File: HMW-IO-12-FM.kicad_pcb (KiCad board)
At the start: 2 copper layers, 47 x 47 mm, 64 parts, among them IC1 ATmega32A-A, IC2 ATmega32A-M, IC3 MAX487E, IC4 MC34063AD, J1 Conn_01x04_Male, J2 Conn_01x04_Male, J3 Screw_Terminal_01x06, J4 BUS_Terminal, Q1 16Mhz

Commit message: Add files via upload
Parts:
- D3: footprint Diode_SMD:D_SMA_Handsoldering -> Diode_SMD:D_MELF
- L1: footprint Inductor_SMD:L_Bourns_SRN6045TA -> Inductor_SMD:L_Taiyo-Yuden_MD-4040
- moved L1 0.65 mm to (145.5, 75.1)
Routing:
- net Net-(D3-Pad1): track 10.6 -> 11.7 mm

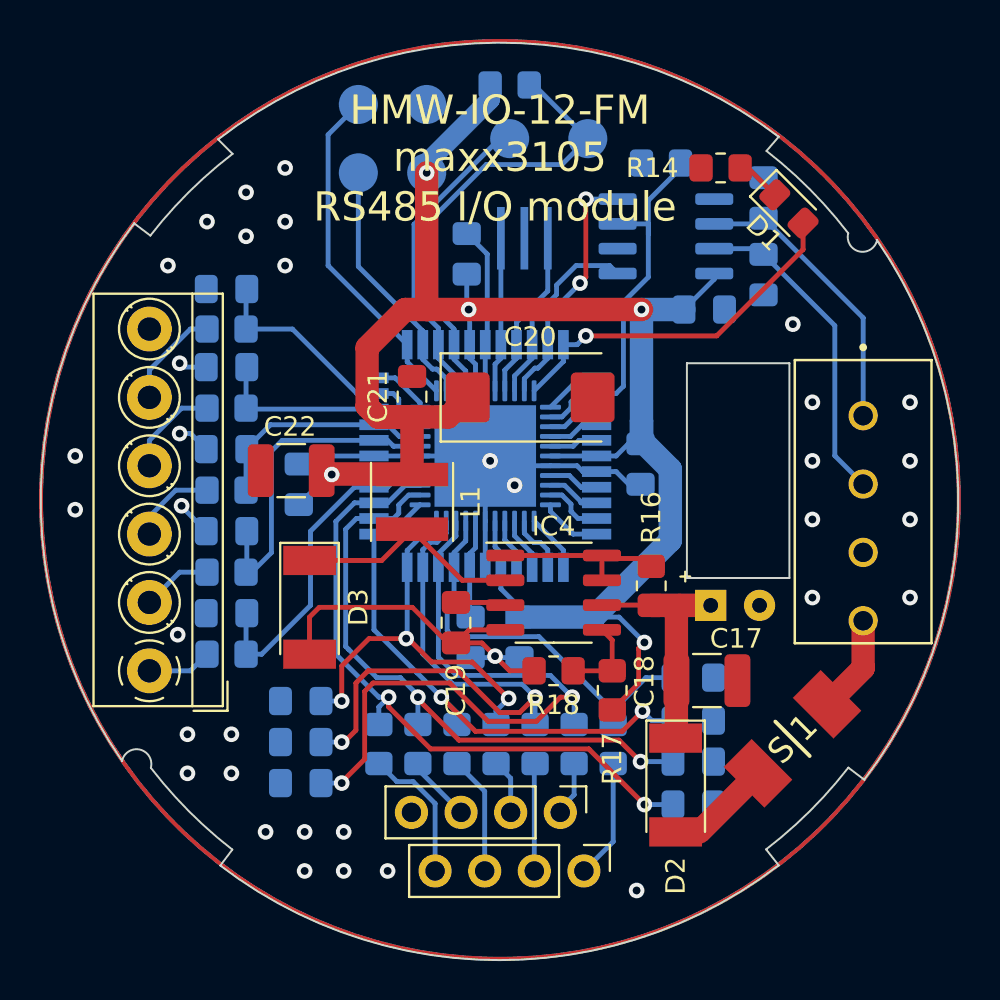
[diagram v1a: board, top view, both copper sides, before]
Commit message: Add files via upload
Bigger hole for tht capacitor.
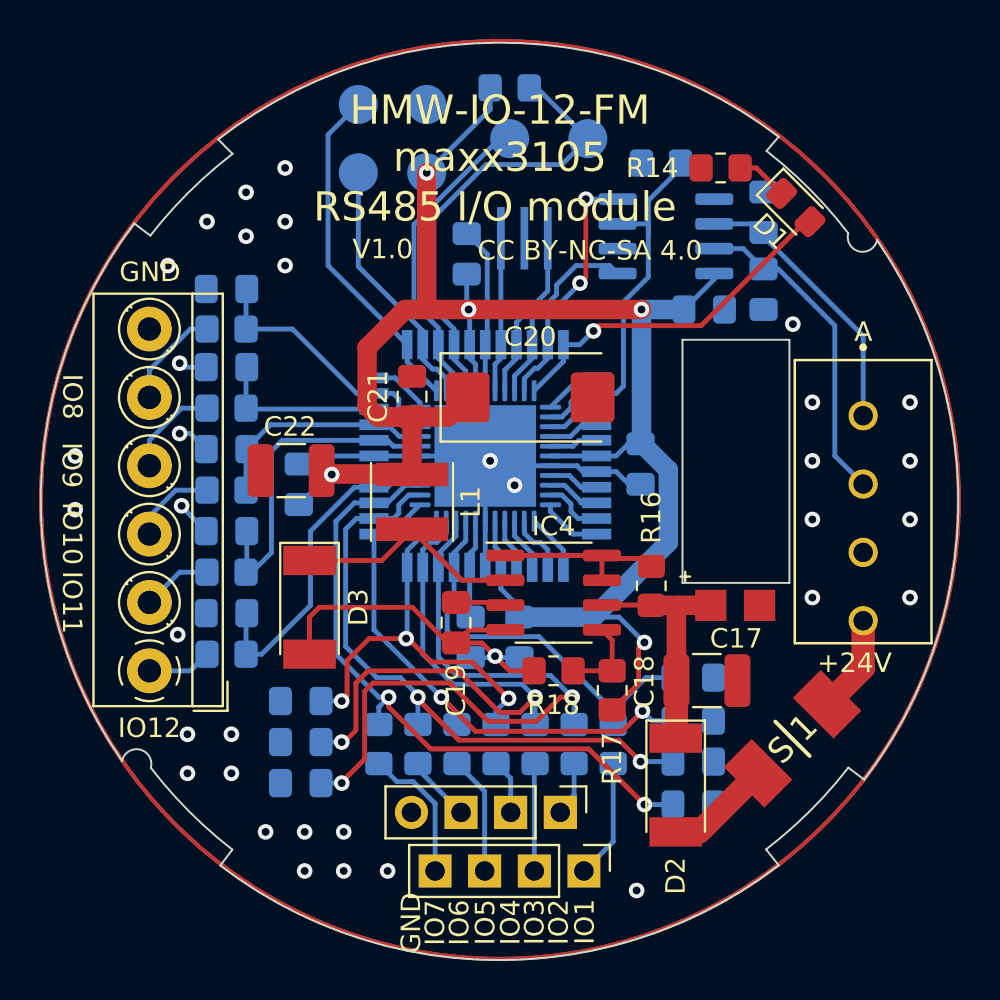
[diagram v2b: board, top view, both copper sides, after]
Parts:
- moved C14 0.75 mm to (163.5, 64.2)
- moved C15 0.73 mm to (163.5, 60.3)
- moved D1 0.36 mm to (165.2, 60.0)
- moved R13 0.15 mm to (150.5, 53.9)
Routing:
- net /GND: track 61.1 -> 58.6 mm
- net /VCC: track 104.0 -> 102.6 mm
- net Net-(D2-Pad2): track 5.46 -> 4.24 mm
- net Net-(J3-Pad3): track 4.31 -> 3.41 mm
- net Net-(C15-Pad1): track 14.9 -> 14.1 mm
- net /SO7: track 34.9 -> 34.2 mm
- net /SCK: track 16.1 -> 15.6 mm
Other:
- outline, holes or cut-outs redrawn
- board text added: "+24V"
- board text added: "A"
- board text added: "CC BY-NC-SA 4.0"
- board text added: "GND"
- board text added: "IO1"
- board text added: "IO10"
- board text added: "IO11"
- board text added: "IO12"
- board text added: "IO2"
- board text added: "IO3"
- board text added: "IO4"
- board text added: "IO5"
- board text added: "IO6"
- board text added: "IO7"
- board text added: "IO8"
- board text added: "IO9"
- board text added: "V1.0"

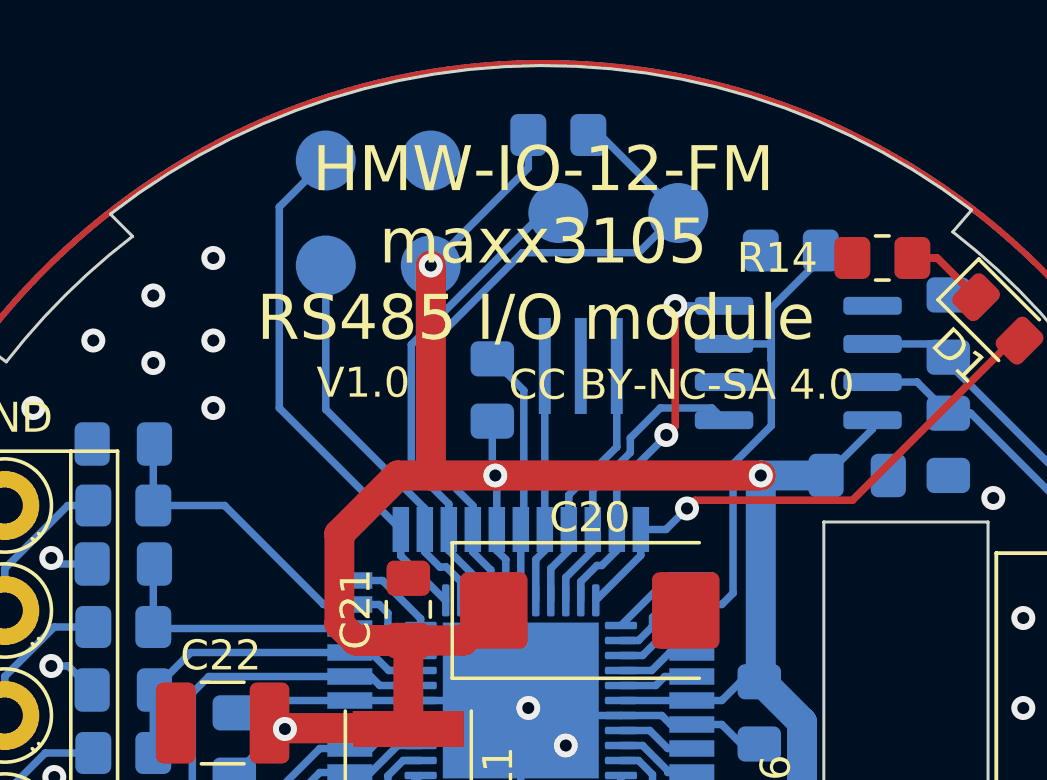
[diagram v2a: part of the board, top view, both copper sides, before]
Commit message: Add button for firmware reset.
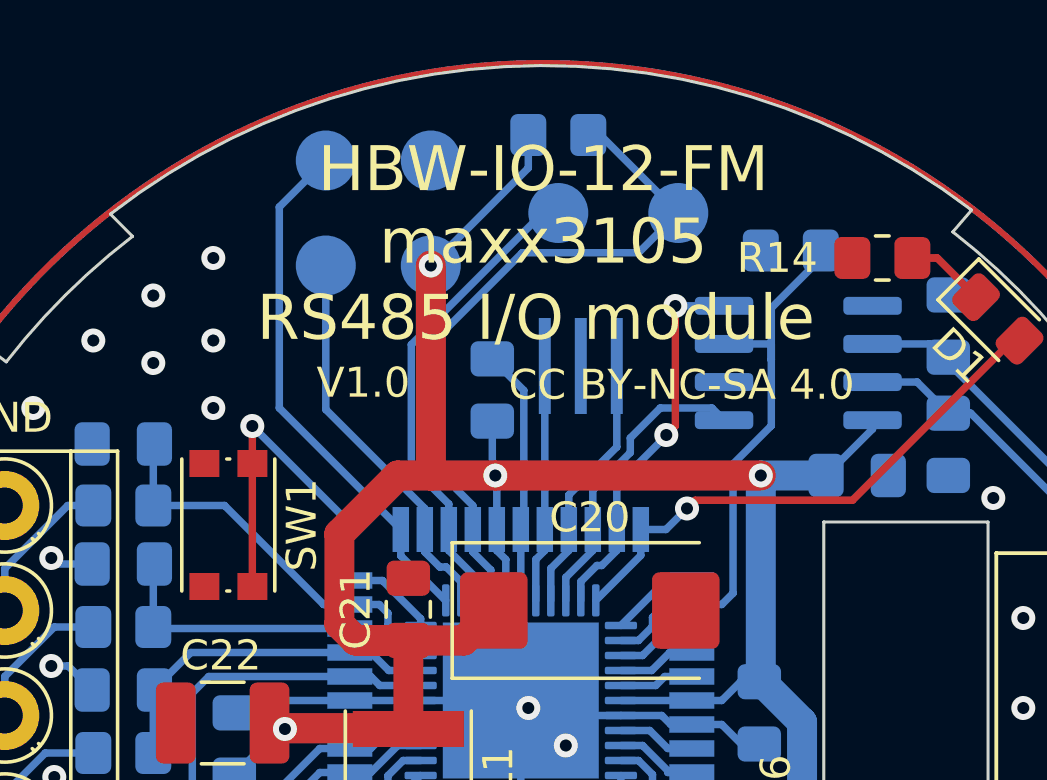
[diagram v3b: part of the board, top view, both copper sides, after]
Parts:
- added SW1: Button, Button_Switch_SMD:SW_Push_1P1T_NO_CK_KMR2, F.Cu at (139.5, 66.9)
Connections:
- net //SS renamed /Button
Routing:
- net /Button: track 3.11 -> 15.0 mm, vias 0 -> 1
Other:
- board text added: "HBW-IO-12-FM maxx3105"
- board text removed: "HMW-IO-12-FM maxx3105"
